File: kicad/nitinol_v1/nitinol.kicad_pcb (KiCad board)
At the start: 2 copper layers, 100 x 100 mm, 109 parts, among them J1 Conn_01x01_Male, J2 PRGM, J4 P1, J6 PRGM, J7 Conn_01x01_Male, Q1 Q_NMOS_GSD, Q2 Q_NMOS_GSD, U1 AP2127K-3.3, U10 WS2811, U2 WS2811, U3 WS2811, U4 EFM8BB10F2G-A-QFN20, U5 WS2811, U6 WS2811, U7 WS2811, U8 WS2811, U9 WS2811

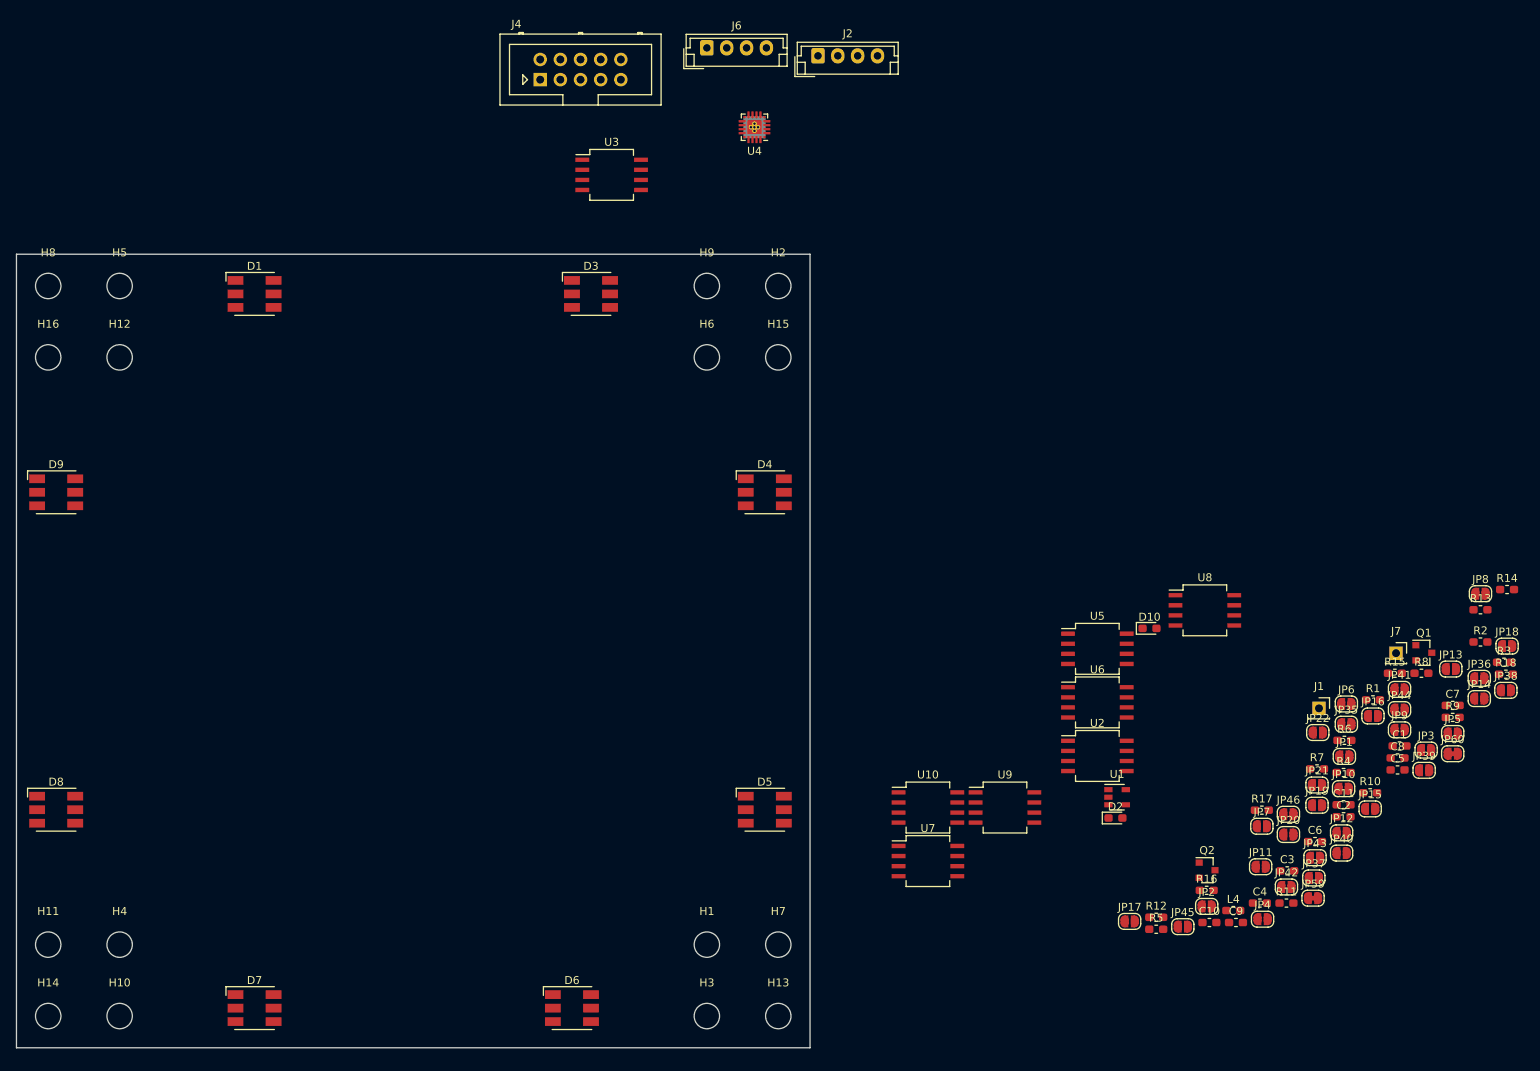
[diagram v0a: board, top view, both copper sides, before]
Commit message: all components placed, starting on tracks
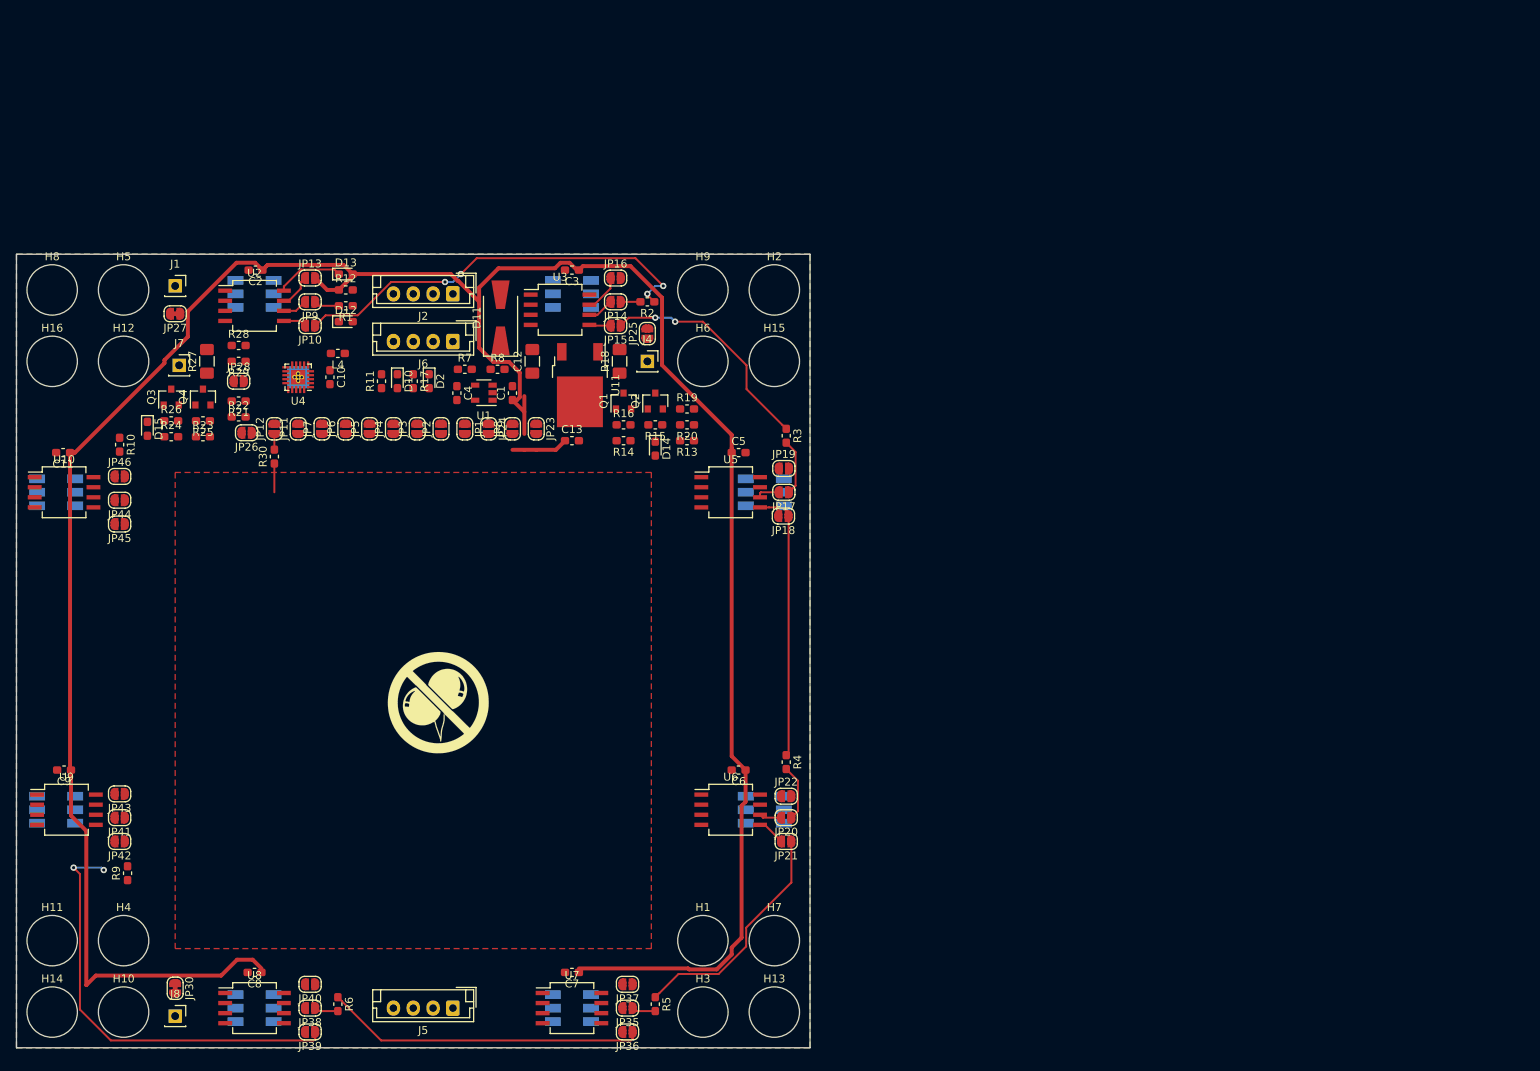
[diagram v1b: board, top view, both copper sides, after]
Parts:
- removed JP59, JP60: Jumper_NC_Small, Jumper:SolderJumper-2_P1.3mm_Bridged_RoundedPad1.0x1.5mm
- added C12: 10uF, Capacitor_SMD:C_1206_3216Metric_Pad1.42x1.75mm_HandSolder, F.Cu at (65.0, 13.5)
- added C13: 10uF, Capacitor_SMD:C_0603_1608Metric_Pad1.05x0.95mm_HandSolder, F.Cu at (70.0, 23.5)
- added D11: 1N5819, Diode_SMD:D_SMA-SMB_Universal_Handsoldering, F.Cu at (61.0, 8.00)
- added D12: JUMPER, Diode_SMD:D_0603_1608Metric_Pad1.05x0.95mm_HandSolder, F.Cu at (41.5, 8.50)
- added D13: JUMPER, Diode_SMD:D_0603_1608Metric_Pad1.05x0.95mm_HandSolder, F.Cu at (41.5, 2.50)
- added D14: RED, LED_SMD:LED_0603_1608Metric_Pad1.05x0.95mm_HandSolder, F.Cu at (80.5, 24.5)
- added D15: RED, LED_SMD:LED_0603_1608Metric_Pad1.05x0.95mm_HandSolder, F.Cu at (16.5, 22.0)
- added J5: OUT, Connector_JST:JST_EH_B04B-EH-A_1x04_P2.50mm_Vertical, F.Cu at (55.0, 95.0)
- added J8: NITINOL_2-, Connector_PinSocket_2.54mm:PinSocket_1x01_P2.54mm_Vertical, F.Cu at (20.0, 96.0)
- added JP23: Jumper_NO_Small, Jumper:SolderJumper-2_P1.3mm_Open_RoundedPad1.0x1.5mm, F.Cu at (65.5, 22.0)
- added JP24: Jumper_NO_Small, Jumper:SolderJumper-2_P1.3mm_Open_RoundedPad1.0x1.5mm, F.Cu at (59.5, 22.0)
- added JP25: Jumper_NO_Small, Jumper:SolderJumper-2_P1.3mm_Open_RoundedPad1.0x1.5mm, F.Cu at (79.5, 10.0)
- added JP26: Jumper_NO_Small, Jumper:SolderJumper-2_P1.3mm_Open_RoundedPad1.0x1.5mm, F.Cu at (29.0, 22.5)
- added JP27: Jumper_NC_Small, Jumper:SolderJumper-2_P1.3mm_Bridged_RoundedPad1.0x1.5mm, F.Cu at (20.0, 7.50)
- added JP28: Jumper_NO_Small, Jumper:SolderJumper-2_P1.3mm_Open_RoundedPad1.0x1.5mm, F.Cu at (28.0, 16.0)
- added JP30: Jumper_NC_Small, Jumper:SolderJumper-2_P1.3mm_Bridged_RoundedPad1.0x1.5mm, F.Cu at (20.0, 92.5)
- added Q3: MMBT3904, Package_TO_SOT_SMD:SOT-23, F.Cu at (19.5, 18.0)
- added Q4: AO3401, Package_TO_SOT_SMD:SOT-23, F.Cu at (23.5, 18.0)
- added R19: 10K 1%, Resistor_SMD:R_0603_1608Metric_Pad1.05x0.95mm_HandSolder, F.Cu at (84.5, 19.5)
- added R20: 10K 1%, Resistor_SMD:R_0603_1608Metric_Pad1.05x0.95mm_HandSolder, F.Cu at (84.5, 21.5)
- added R21: 10K 1%, Resistor_SMD:R_0603_1608Metric_Pad1.05x0.95mm_HandSolder, F.Cu at (28.0, 18.5)
- added R22: 10K 1%, Resistor_SMD:R_0603_1608Metric_Pad1.05x0.95mm_HandSolder, F.Cu at (28.0, 20.5)
- added R23: 100K, Resistor_SMD:R_0603_1608Metric_Pad1.05x0.95mm_HandSolder, F.Cu at (23.5, 23.0)
- added R24: 1K, Resistor_SMD:R_0603_1608Metric_Pad1.05x0.95mm_HandSolder, F.Cu at (19.5, 23.0)
- added R25: 10K 1%, Resistor_SMD:R_0603_1608Metric_Pad1.05x0.95mm_HandSolder, F.Cu at (23.5, 21.0)
- added R26: 10K 1%, Resistor_SMD:R_0603_1608Metric_Pad1.05x0.95mm_HandSolder, F.Cu at (19.5, 21.0)
- added R27: 1R, Resistor_SMD:R_1206_3216Metric_Pad1.42x1.75mm_HandSolder, F.Cu at (24.0, 13.5)
- added R28: 10K 1%, Resistor_SMD:R_0603_1608Metric_Pad1.05x0.95mm_HandSolder, F.Cu at (28.0, 11.5)
- added R29: 10K 1%, Resistor_SMD:R_0603_1608Metric_Pad1.05x0.95mm_HandSolder, F.Cu at (28.0, 13.5)
- added R30: 1K, Resistor_SMD:R_0603_1608Metric_Pad1.05x0.95mm_HandSolder, F.Cu at (32.5, 25.5)
- added SYM1: SYM_Radioactive_Radiation_Small, logo:logo_large, F.Cu at (53.5, 56.5)
- added U11: LM1117-5.0, Package_TO_SOT_SMD:TO-252-2, F.Cu at (71.0, 16.5)
- D1, D3, D4, D5, D6, D7, D8, D9: moved to B.Cu
- H1, H10, H11, H12, H13, H14, H15, H16, H2, H3, H4, H5, H6, H7, H8, H9: footprint MountingHole:MountingHole_3.2mm_M3 -> parts:Grommet_0.25in_1061T11
- J1: value Conn_01x01_Male -> NITINOL_1-
- J2: value PRGM -> IN
- J4: value P1 -> NITINOL_1+; footprint Connector_Multicomp:Multicomp_MC9A12-1034_2x05_P2.54mm_Vertical -> Connector_PinSocket_2.54mm:PinSocket_1x01_P2.54mm_Vertical
- J7: value Conn_01x01_Male -> NITINOL_2+
- Q1: value Q_NMOS_GSD -> MMBT3904
- Q2: value Q_NMOS_GSD -> AO3401
- R12: value 10K 1% -> NC
- R13: value 10K 1% -> 100K
- R14: value 16K 1% -> 1K
- R18: value 16K 1% -> 1R; footprint Resistor_SMD:R_0603_1608Metric_Pad1.05x0.95mm_HandSolder -> Resistor_SMD:R_1206_3216Metric_Pad1.42x1.75mm_HandSolder
- U4: footprint Package_DFN_QFN:SiliconLabs_QFN-20-1EP_3x3mm_P0.5mm_ThermalVias -> parts:SiliconLabs_QFN-20-1EP_3x3mm_P0.5mm_ThermalVias
- moved R9 168.1 mm to (14.0, 78.0), turned to 90 degrees
- moved C11 167.4 mm to (5.88, 25.0), turned to 180 degrees
- moved R10 163.6 mm to (13.0, 24.0), turned to 270 degrees
- moved JP44 163.4 mm to (13.0, 31.0), turned to 180 degrees
- moved JP41 162.1 mm to (13.0, 71.0), turned to 180 degrees
- moved J7 157.6 mm to (20.5, 14.0)
- moved JP38 155.9 mm to (37.0, 95.0), turned to 180 degrees
- moved J1 153.6 mm to (20.0, 4.00)
- moved C2 153.4 mm to (30.1, 2.00), turned to 180 degrees
- moved JP46 153.3 mm to (13.0, 28.0)
- moved JP13 152.0 mm to (37.0, 3.00)
- moved JP43 150.8 mm to (13.0, 68.0), turned to 180 degrees
- moved C9 148.9 mm to (6.00, 65.0), turned to 180 degrees
- moved JP9 147.5 mm to (37.0, 6.00), turned to 180 degrees
- moved JP42 147.1 mm to (13.0, 74.0), turned to 180 degrees
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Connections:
- J1 pad 1: Net-(J1-Pad1) -> /N1_d
- J2 pad 1: +3V3 -> VDD
- J2 pad 2: /DI -> GND
- J2 pad 3: /DO -> /DI
- J2 pad 4: GND -> /DO
- J4 pad 1: +3V3 -> /N2_c
- J7 pad 1: Net-(J7-Pad1) -> /N2_c
- Q1 pad 1: /NITINOL_1 -> Net-(Q1-Pad1)
- Q1 pad 3: Net-(JP59-Pad2) -> Net-(Q1-Pad3)
- Q2 pad 1: /NITINOL_1 -> Net-(Q1-Pad3)
- Q2 pad 2: GND -> /N1_a
- Q2 pad 3: Net-(JP60-Pad2) -> /N1_b
- R1 pad 1: /DATA -> Net-(D12-Pad2)
- R11 pad 1: /P1.0 -> /P1.1
- R12 pad 1: /SENSE_1 -> +5V
- R12 pad 2: GND -> Net-(D12-Pad2)
- R13 pad 1: /SENSE_1 -> /NITINOL_1
- R13 pad 2: Net-(JP59-Pad2) -> Net-(D14-Pad2)
- R14 pad 1: /NITINOL_1 -> Net-(Q1-Pad1)
- R14 pad 2: GND -> /NITINOL_1
- R15 pad 1: /SENSE_1 -> /N1_a
- R15 pad 2: GND -> Net-(Q1-Pad3)
- R16 pad 1: /SENSE_1 -> Net-(Q1-Pad1)
- R16 pad 2: Net-(JP60-Pad2) -> GND
- R17 pad 1: +3V3 -> Net-(JP24-Pad2)
- R18 pad 1: /NITINOL_1 -> /N1_b
- R18 pad 2: GND -> /N2_c
- U2 pad 8: +5V -> Net-(D13-Pad1)
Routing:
- net +5V: track 0.00 -> 330.9 mm
- net Net-(JP39-Pad1): track 0.00 -> 54.3 mm, vias 0 -> 2
- net Net-(JP10-Pad1): track 0.00 -> 52.6 mm, vias 0 -> 4
- net Net-(JP36-Pad1): track 0.00 -> 40.3 mm
- net Net-(JP18-Pad1): track 0.00 -> 30.2 mm
- net Net-(JP21-Pad1): track 0.00 -> 29.7 mm
- net Net-(JP15-Pad1): track 0.00 -> 28.8 mm, vias 0 -> 2
- net Net-(D13-Pad1): track 0.00 -> 8.58 mm
- net Net-(JP17-Pad1): track 0.00 -> 7.08 mm
- net Net-(JP20-Pad1): track 0.00 -> 7.08 mm
- net Net-(JP16-Pad1): track 0.00 -> 4.81 mm
- net Net-(JP13-Pad1): track 0.00 -> 4.31 mm
- net CAPACITIVE_TOUCH: track 0.00 -> 3.62 mm
- net Net-(JP21-Pad2): track 0.00 -> 3.54 mm
- net Net-(JP14-Pad2): track 0.00 -> 3.33 mm
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- added copper zone on F.Cu, net CAPACITIVE_TOUCH
- added copper zone on B.Cu, net GND
- added copper zone on F.Cu, net GND
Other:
- net class PWR added: clearance 0.2, trace_width 0.5, via_dia 0.8, via_drill 0.4
